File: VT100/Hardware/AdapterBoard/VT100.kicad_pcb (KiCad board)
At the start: 2 copper layers, 99.7 x 99.6 mm, 40 parts, among them J1 GPIO, J2 RS232, J3 Vin < 12V DC / AC, J4 Mini-DIN-6, J5 zu Pi Zero, J6 USB_A, J7 Z80-MBC2 direct, J8 LCD Power, J9 On / Off, K1 G5V-2, Q2 BC546, Q3 BS170, U1 LM2576HVS-ADJ

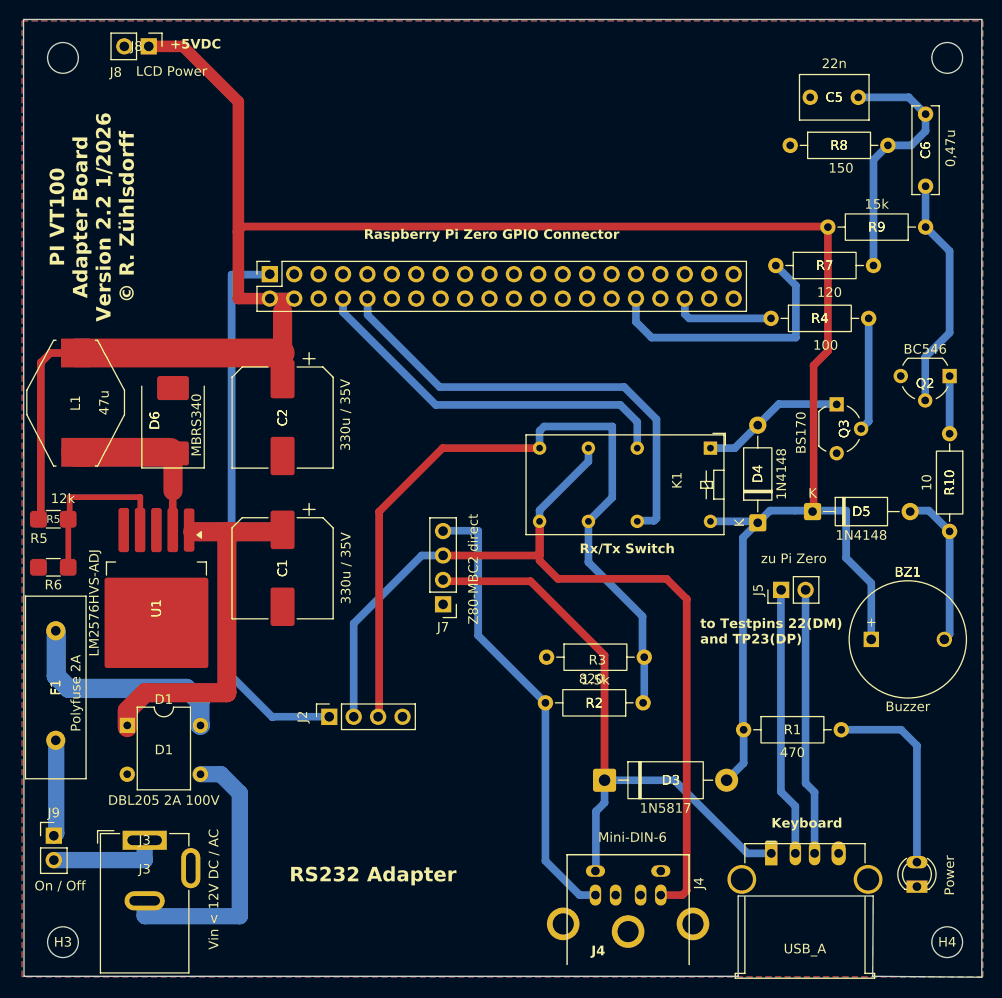
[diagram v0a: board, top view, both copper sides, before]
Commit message: VT100 AdapterBoard: add TxD level shifter
Add TxD level shifting network in AdapterBoard schematic and PCB routing.\n\nChanges include new resistor-based shift path and corresponding net/routing updates for TXD signal adaptation.
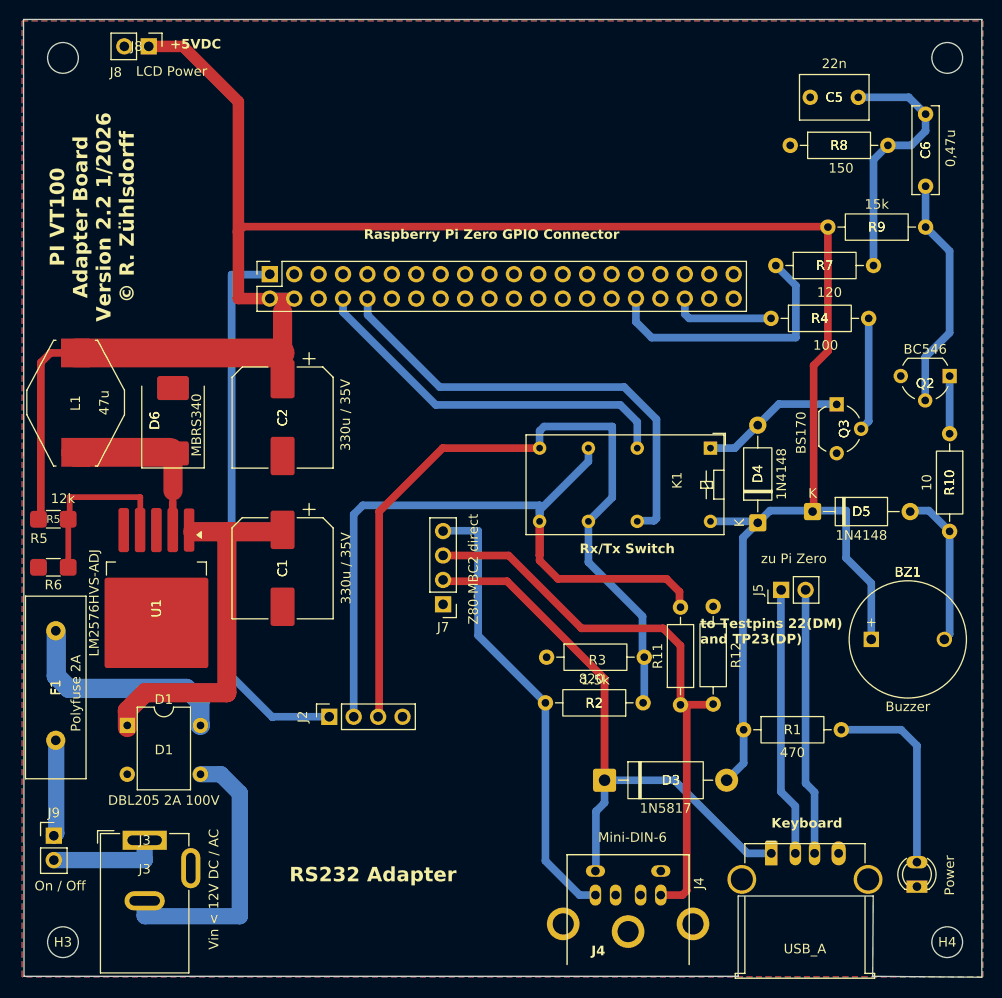
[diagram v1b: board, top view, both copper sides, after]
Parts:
- added R11: 820, Resistor_THT:R_Axial_DIN0207_L6.3mm_D2.5mm_P10.16mm_Horizontal, F.Cu at (167.5, 140.2)
- added R12: 1.5k, Resistor_THT:R_Axial_DIN0207_L6.3mm_D2.5mm_P10.16mm_Horizontal, F.Cu at (170.9, 130.0)
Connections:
- J4 pad 3: Net-(J2-Pin_2) -> Net-(J7-Pin_3)
- J7 pad 3: Net-(J2-Pin_2) -> Net-(J7-Pin_3)
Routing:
- net Net-(J7-Pin_3): track 0.00 -> 61.4 mm
- net Net-(J2-Pin_2): track 99.5 -> 77.3 mm
- net Net-(D3-K): track 63.4 -> 62.0 mm
